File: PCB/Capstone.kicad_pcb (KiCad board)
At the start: 4 copper layers, 86.4 x 68.6 mm, 237 parts, among them J1 S2B-PH-SM4-TB, J10 DNP, J11 DNP, J12 DNP, J2 TRANSDUCER, J3 DNP, J4 PH1-08-UA, J5 DNP, J6 DNP, J7 DNP, J8 PH1-08-UA, J9 DNP, Q1 SSM6K361NU, SW1 SW_Push, SW2 SW_Push, SW3 SW_Push, U1 TPS63031, U10 AP2204K-ADJ, U11 LM3478, U12 10CL010, U13 ECS-5032MV, U14 TSX9291, U15 LTC6090-5, U16 AD5450, U17 ADA4522-1, U18 MAX5394L, U19 MAX5394L, U2 TCR2EF25, U20 MAX11116, U21 TLV3544, U22 MCP6L1, U3 TPS62262, U4 BMD-360, U5 MIC841N, U6 ENS210, U7 W25Q80DV, U8 LIS2DE12, U9 LMR62421

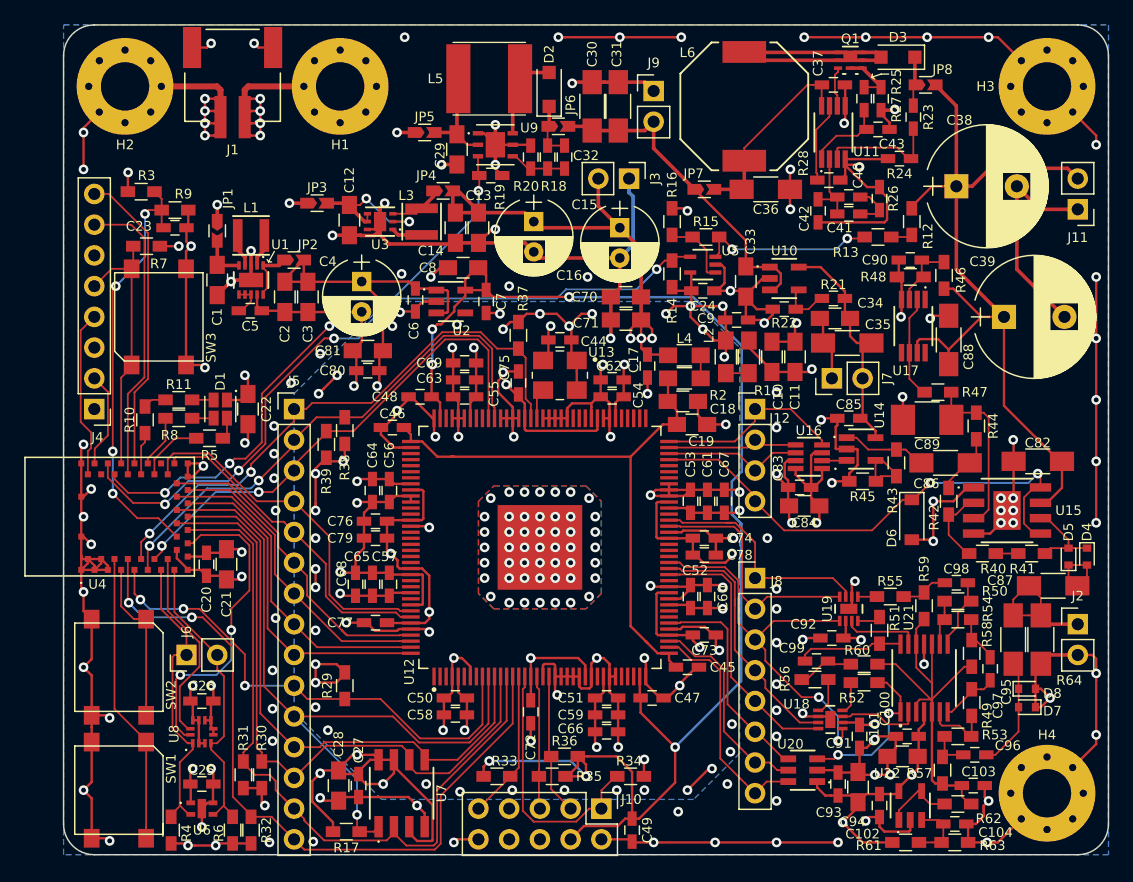
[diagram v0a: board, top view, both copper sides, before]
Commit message: Adjust receive circuit to increase stability (hopefully less likely to oscillate)
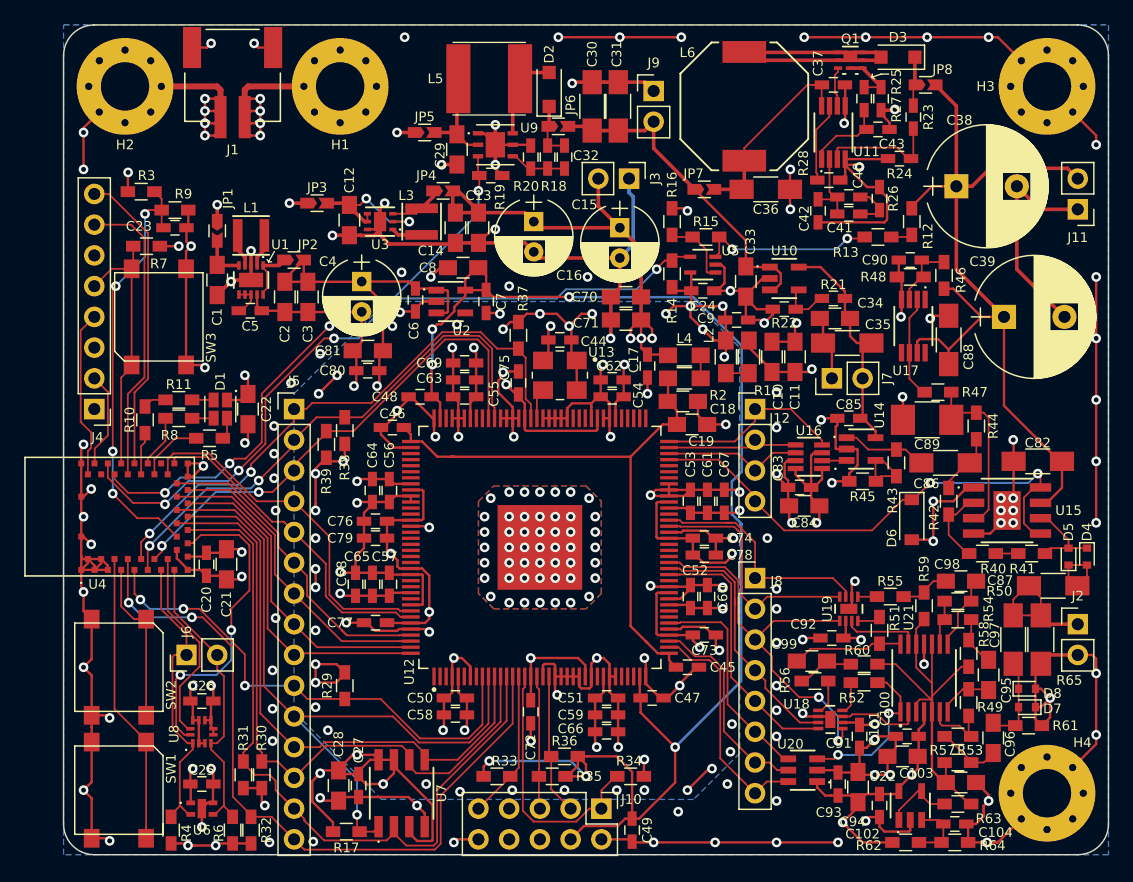
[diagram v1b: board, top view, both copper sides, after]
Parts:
- added R61: 1k, Resistors_SMD:R_0603_HandSoldering, F.Cu at (166.1, 153.2)
- C103: value 4.7uF -> 10uF; footprint Capacitors_SMD:C_0603_HandSoldering -> Capacitors_SMD:C_0805_HandSoldering
- C96, C97, C98, C99: value 150nF -> 68nF; footprint Capacitors_SMD:C_0603_HandSoldering -> Capacitors_SMD:C_0805_HandSoldering
- R57, R58, R59, R60: value 1k -> 10k
- R63: renamed from R62; value 10 -> 1
- moved C96 2.07 mm to (163.2, 154.2), turned to 270 degrees
- moved R57 1.42 mm to (160.3, 156.2), turned to 180 degrees
- moved C103 1.05 mm to (160.5, 157.9)
- moved C97 0.52 mm to (162.8, 149.0)
- moved C98 0.40 mm to (160.5, 141.2)
- moved C99 0.38 mm to (148.2, 147.8)
- moved R49 0.25 mm to (161.2, 151.3)
- moved R58 0.25 mm to (161.2, 147.2)
- moved R56 0.13 mm to (148.5, 149.5)
- renumbered R61 to R62, R63 to R64, R64 to R65
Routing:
- net GND: track 601.9 -> 606.8 mm
- net Net-(C96-Pad2): track 3.31 -> 5.30 mm
- net Net-(C95-Pad1): track 9.25 -> 7.33 mm
- net /Receive/MIDRAIL: track 36.0 -> 36.8 mm

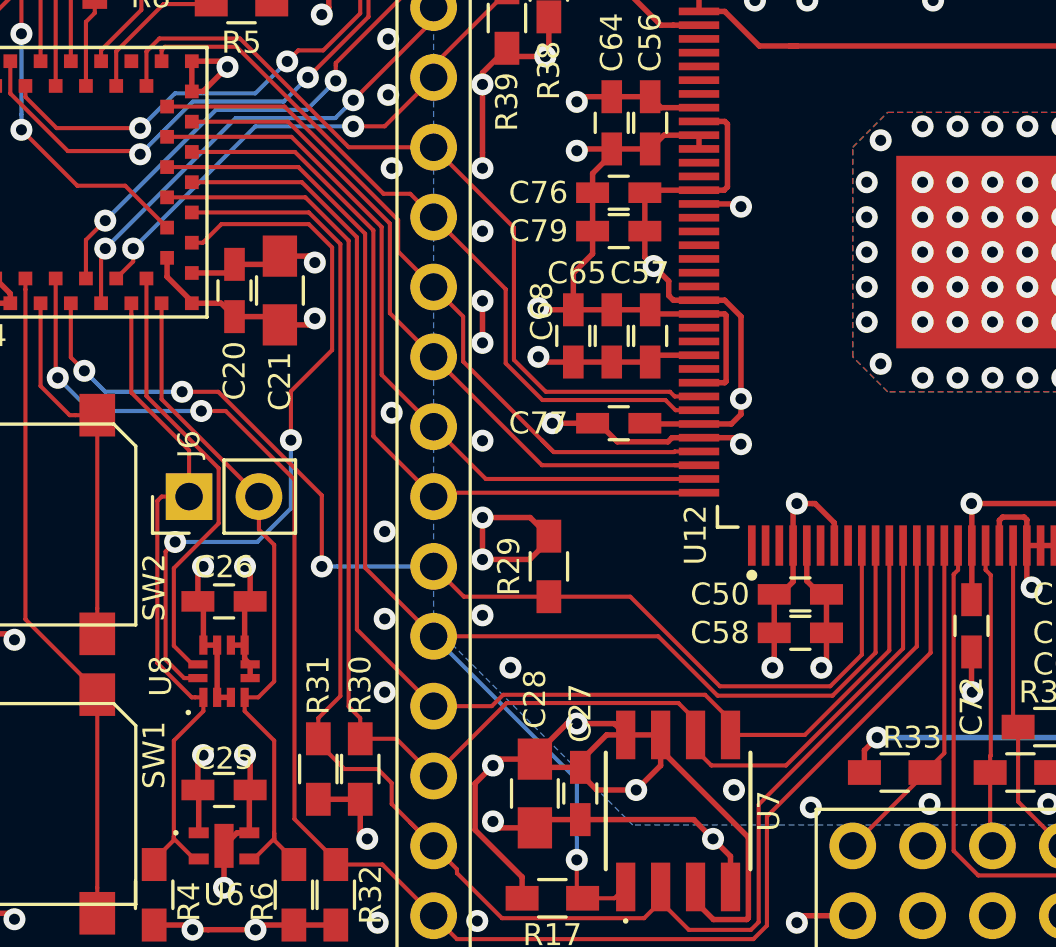
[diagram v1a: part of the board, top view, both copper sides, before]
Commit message: Move FPGA SPI-DOUT pin to make Quartus happy
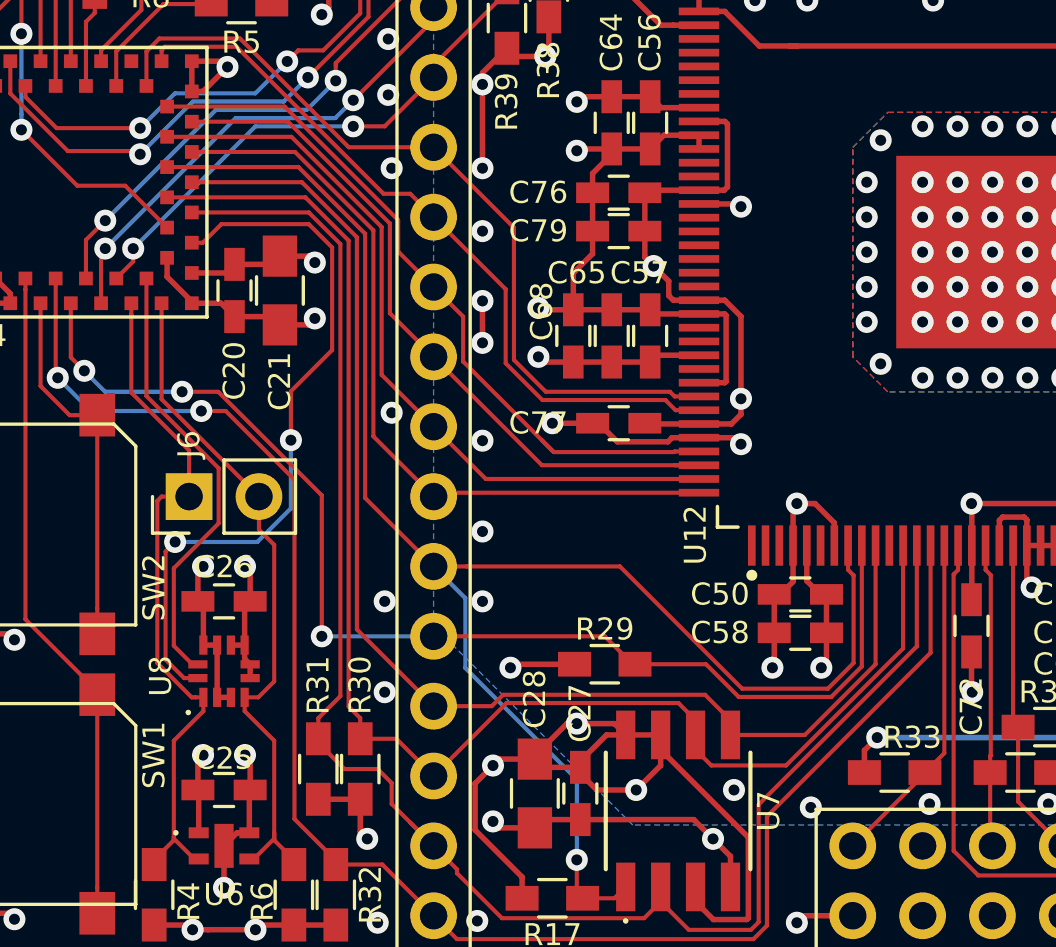
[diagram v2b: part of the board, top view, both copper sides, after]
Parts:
- moved R29 4.10 mm to (111.6, 153.4), turned to 180 degrees
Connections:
- J5 pad 10: FPGA-nSTATUS -> FPGA-CS
- J5 pad 11: FPGA-CS -> FPGA-nSTATUS
- U12 pad 10: FPGA-CS -> FPGA-DOUT
- U12 pad 11: FPGA-DOUT -> Net-(U12-Pad11)
- U12 pad 8: Net-(U12-Pad8) -> FPGA-CS
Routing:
- net +3V3: track 207.8 -> 203.1 mm, vias 52 -> 51
- net FPGA-nSTATUS: track 41.6 -> 43.7 mm
- net GND: vias 205 -> 204
